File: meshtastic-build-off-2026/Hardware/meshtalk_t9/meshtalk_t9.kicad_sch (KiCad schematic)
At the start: 0 parts

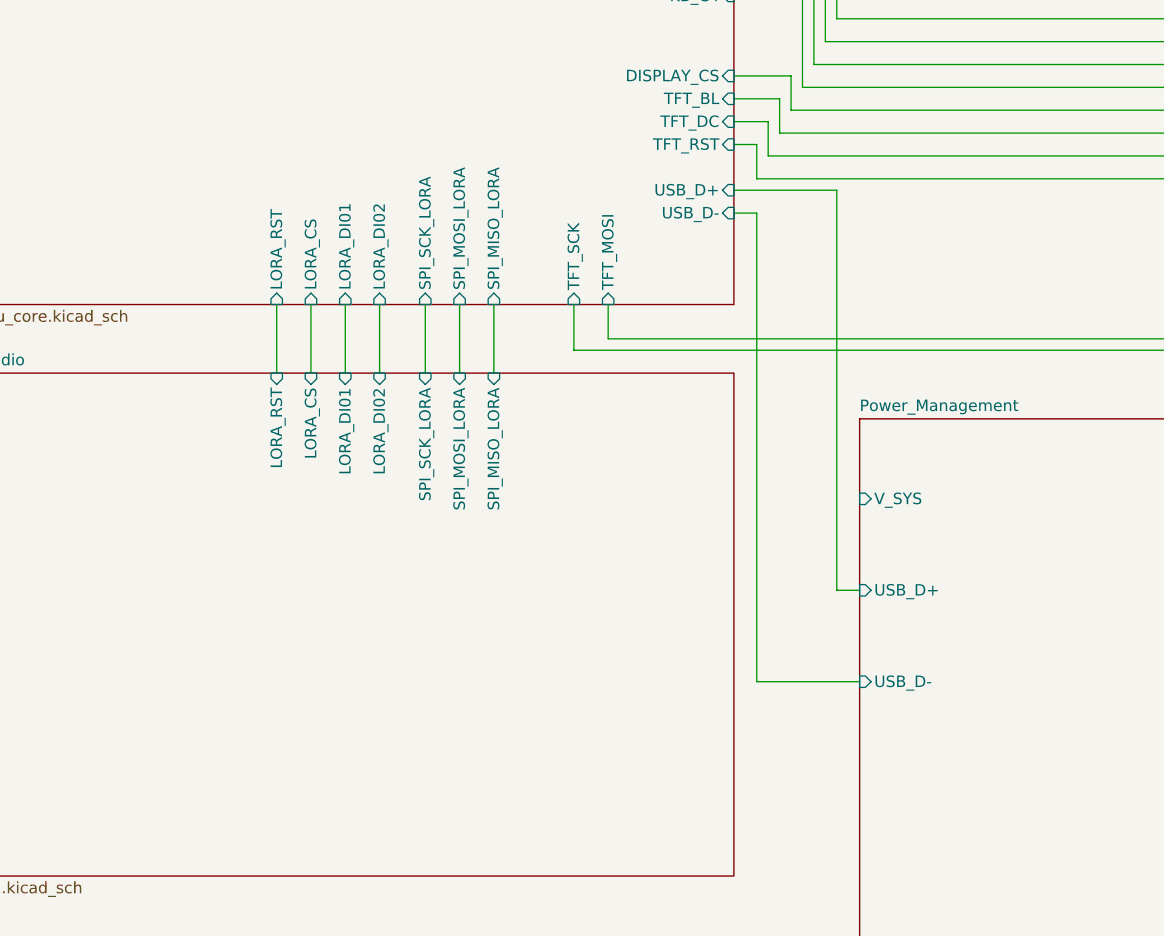
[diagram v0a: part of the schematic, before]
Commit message: rename + battery % + boot btn changed to reset + fix battery chrging
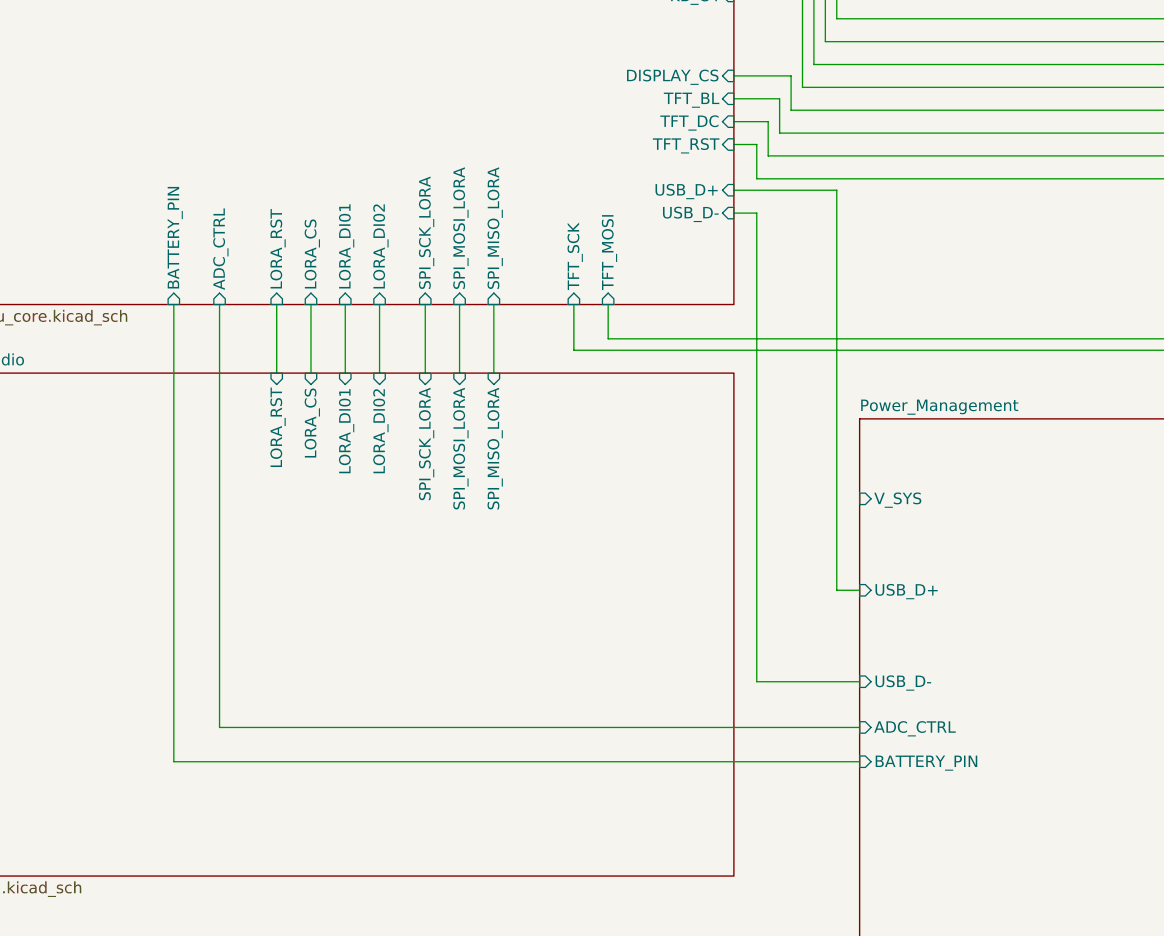
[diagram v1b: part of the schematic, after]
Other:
- sheet MCU_Core ports: added ADC_CTRL, BATTERY_PIN; removed none
- sheet Power_Management ports: added ADC_CTRL, BATTERY_PIN; removed none
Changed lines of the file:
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@@
+	(wire
+		(pts
+			(xy 39.37 121.92) (xy 115.57 121.92)
+		)
+		(stroke
+			(width 0)
+			(type default)
+		)
+	)
+	(wire
+		(pts
+			(xy 44.45 71.12) (xy 44.45 118.11)
+		)
+		(stroke
+			(width 0)
+			(type default)
+		)
+	)
 	(wire
 		(pts
@@
 	(wire
 		(pts
+			(xy 39.37 71.12) (xy 39.37 121.92)
+		)
+		(stroke
+			(width 0)
+			(type default)
+		)
+	)
+	(wire
+		(pts
 			(xy 110.49 34.29) (xy 101.6 34.29)
 		)
@@
 		(pts
 			(xy 114.3 36.83) (xy 172.72 36.83)
+		)
+		(stroke
+			(width 0)
+			(type default)
+		)
+	)
+	(wire
+		(pts
+			(xy 44.45 118.11) (xy 115.57 118.11)
 		)
 		(stroke
@@
 			)
 		)
+		(pin "BATTERY_PIN" input
+			(at 115.57 121.92 180)
+			(effects
+				(font
+					(size 1.27 1.27)
+				)
+				(justify left)
+			)
+		)
+		(pin "ADC_CTRL" input
+			(at 115.57 118.11 180)
+			(effects
+				(font
+					(size 1.27 1.27)
+				)
+				(justify left)
+			)
+		)
 		(instances
 			(project "Untitled"
@@
 			(effects
 				(font
+					(size 1.27 1.27)
+				)
+				(justify left)
+			)
+		)
+		(pin "ADC_CTRL" input
+			(at 44.45 71.12 270)
+			(effects
+				(font
+					(size 1.27 1.27)
+				)
+				(justify left)
+			)
+		)
+		(pin "BATTERY_PIN" input
+			(at 39.37 71.12 270)
+			(effects
+				(font

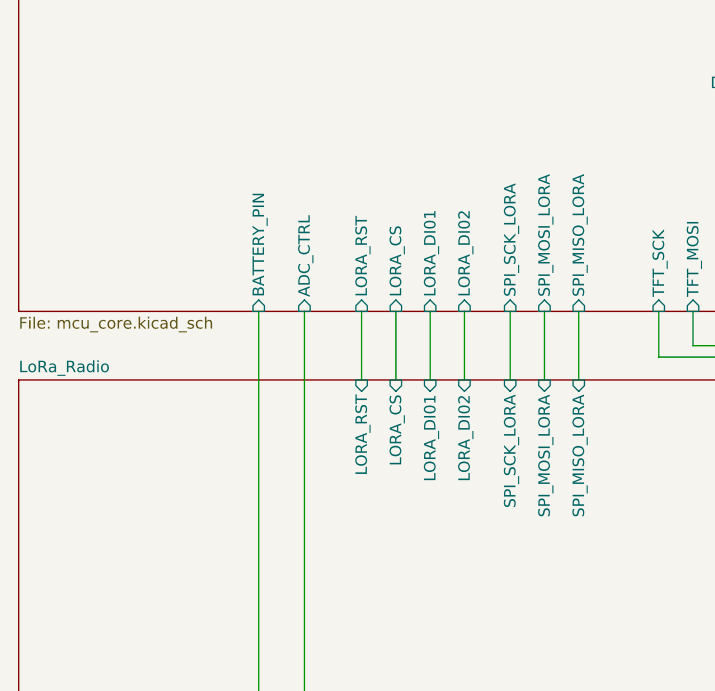
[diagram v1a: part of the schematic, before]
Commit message: Replace AP2112K-3.3  with AP7361C-33E Connected LORA RF_SW1 to GPIO Added ESD Added mounting holes for display (Waveshare 2 inch) Added Boot and Reset buttons made power rails thicker added dedicated layer for 3v3 and GND
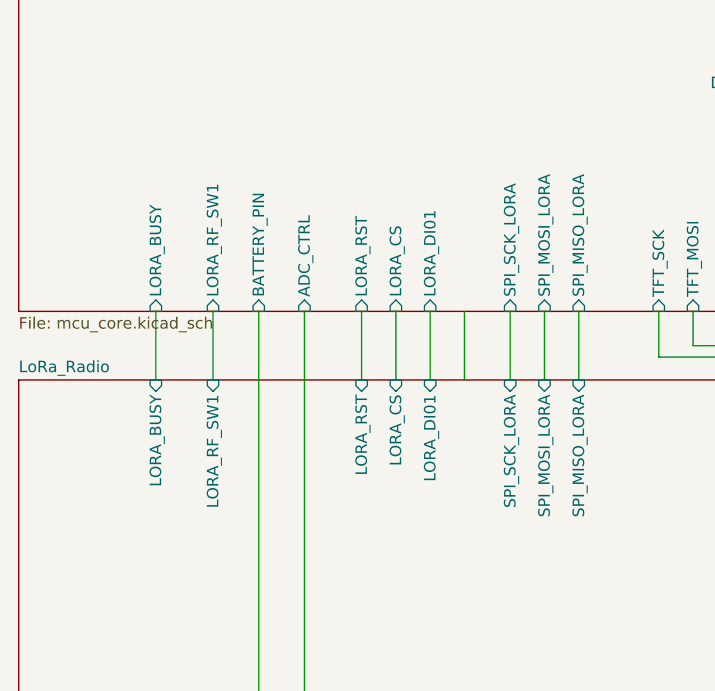
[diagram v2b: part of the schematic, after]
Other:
- sheet LoRa_Radio ports: added LORA_BUSY, LORA_RF_SW1; removed LORA_DI02
- sheet MCU_Core ports: added LORA_BUSY, LORA_RF_SW1; removed LORA_DI02
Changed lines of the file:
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@@
+	(wire
+		(pts
+			(xy 27.94 71.12) (xy 27.94 78.74)
+		)
+		(stroke
+			(width 0)
+			(type default)
+		)
+	)
 	(wire
 		(pts
@@
 		(pts
 			(xy 116.84 21.59) (xy 101.6 21.59)
+		)
+		(stroke
+			(width 0)
+			(type default)
+		)
+	)
+	(wire
+		(pts
+			(xy 34.29 71.12) (xy 34.29 78.74)
 		)
 		(stroke
@@
 			)
 		)
-		(pin "LORA_DI02" input
-			(at 62.23 78.74 90)
-			(effects
-				(font
-					(size 1.27 1.27)
-				)
-				(justify right)
-			)
-		)
 		(pin "LORA_DI01" input
 			(at 58.42 78.74 90)
@@
 			)
 		)
+		(pin "LORA_RF_SW1" input
+			(at 34.29 78.74 90)
+			(effects
+				(font
+					(size 1.27 1.27)
+				)
+				(justify right)
+			)
+		)
+		(pin "LORA_BUSY" input
+			(at 27.94 78.74 90)
+			(effects
+				(font
+					(size 1.27 1.27)
+				)
+				(justify right)
+			)
+		)
 		(instances
-			(project "Untitled"
+			(project "meshtalk_t9"
 				(path "/81d8a60b-fb85-4750-b4ba-90a418a69e1e"
 					(page "4")
@@
 		)
 		(instances
-			(project "Untitled"
+			(project "meshtalk_t9"
 				(path "/81d8a60b-fb85-4750-b4ba-90a418a69e1e"
 					(page "5")
@@
 		)
 		(instances
-			(project "Untitled"
+			(project "meshtalk_t9"
 				(path "/81d8a60b-fb85-4750-b4ba-90a418a69e1e"
 					(page "3")
@@
 			)
 		)
-		(pin "LORA_DI02" input
-			(at 62.23 71.12 270)
-			(effects
-				(font
-					(size 1.27 1.27)
-				)
-				(justify left)
-			)
-		)
 		(pin "KB_R1" input
 			(at 101.6 19.05 0)
@@
 			)
 		)
+		(pin "LORA_RF_SW1" input
+			(at 34.29 71.12 270)
+			(effects
+				(font
+					(size 1.27 1.27)
+				)
+				(justify left)
+			)
+		)
+		(pin "LORA_BUSY" input
+			(at 27.94 71.12 270)
+			(effects
+				(font
+					(size 1.27 1.27)
+				)
+				(justify left)
+			)
+		)
 		(instances
-			(project "Untitled"
+			(project "meshtalk_t9"
 				(path "/81d8a60b-fb85-4750-b4ba-90a418a69e1e"
 					(page "2")

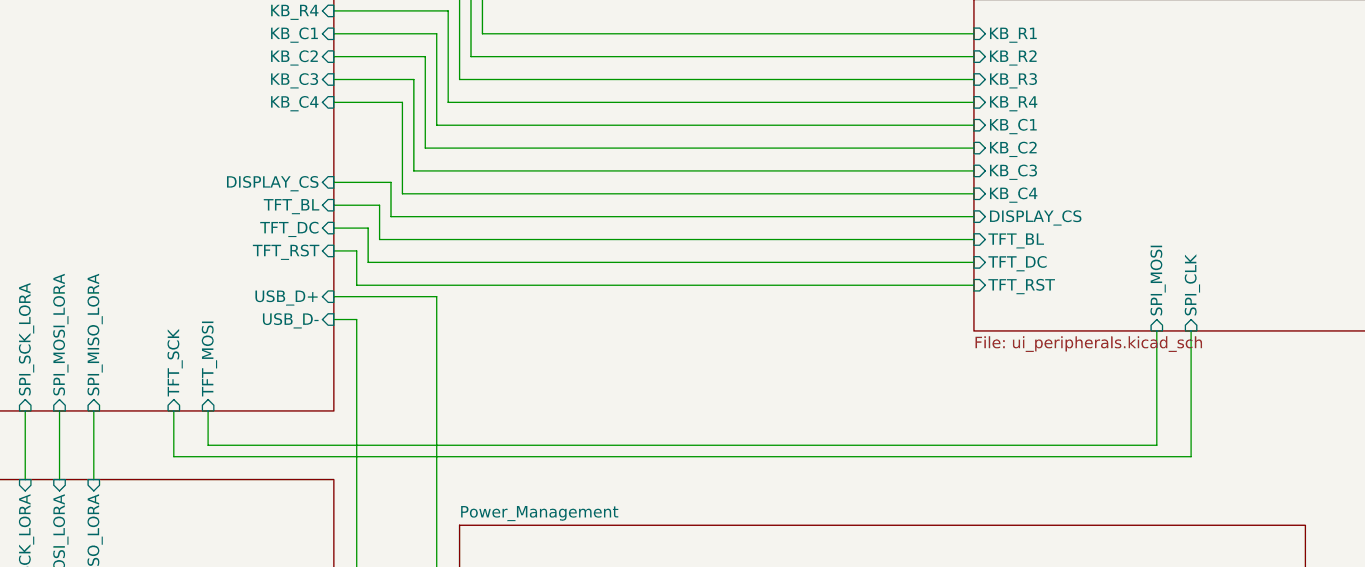
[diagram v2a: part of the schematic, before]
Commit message: PCB Updates - Align net names Clearence for esp32 antenna
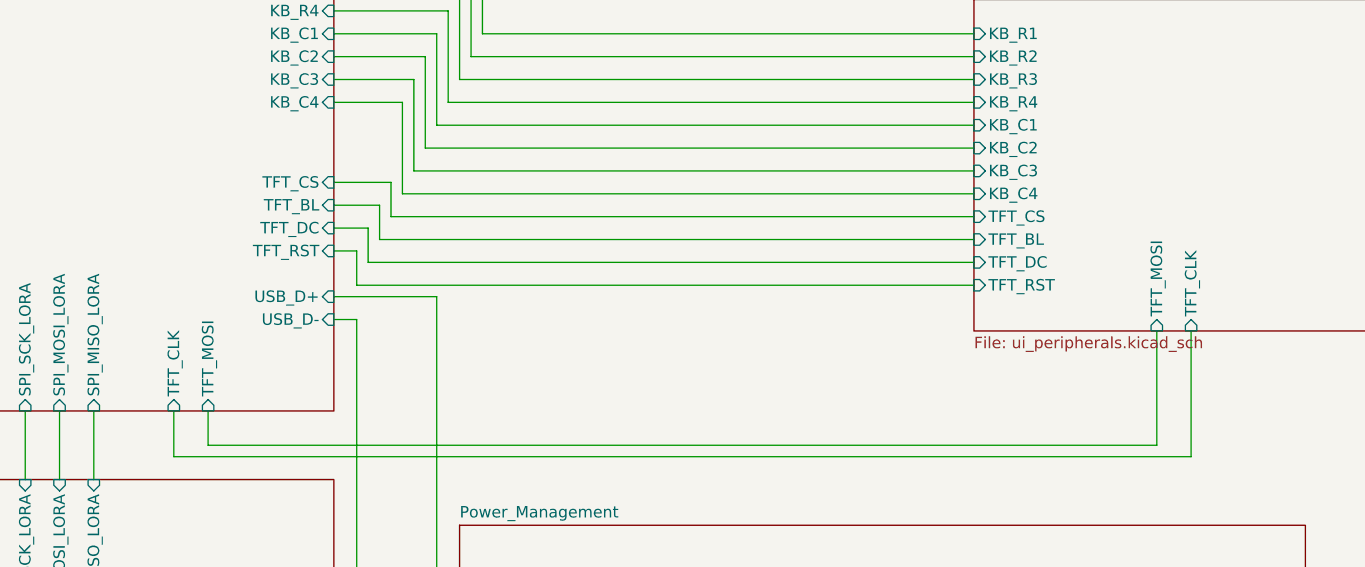
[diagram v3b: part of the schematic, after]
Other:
- sheet MCU_Core ports: added TFT_CLK, TFT_CS; removed DISPLAY_CS, TFT_SCK
- sheet User_Interface ports: added TFT_CLK, TFT_CS, TFT_MOSI; removed DISPLAY_CS, SPI_CLK, SPI_MOSI
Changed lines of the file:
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@@
-			)
-		)
-		(pin "SPI_MOSI" input
-			(at 193.04 62.23 270)
-			(effects
-				(font
-					(size 1.27 1.27)
-				)
-				(justify left)
 			)
 		)
@@
 			)
 		)
-		(pin "DISPLAY_CS" input
-			(at 172.72 49.53 180)
-			(effects
-				(font
-					(size 1.27 1.27)
-				)
-				(justify left)
-			)
-		)
 		(pin "TFT_BL" input
 			(at 172.72 52.07 180)
@@
 			)
 		)
-		(pin "SPI_CLK" input
+		(pin "TFT_MOSI" input
+			(at 193.04 62.23 270)
+			(effects
+				(font
+					(size 1.27 1.27)
+				)
+				(justify left)
+			)
+		)
+		(pin "TFT_CLK" input
 			(at 196.85 62.23 270)
+			(effects
+				(font
+					(size 1.27 1.27)
+				)
+				(justify left)
+			)
+		)
+		(pin "TFT_CS" input
+			(at 172.72 49.53 180)
 			(effects
 				(font
@@
 			)
 		)
-		(pin "DISPLAY_CS" input
-			(at 101.6 45.72 0)
-			(effects
-				(font
-					(size 1.27 1.27)
-				)
-				(justify right)
-			)
-		)
 		(pin "TFT_BL" input
 			(at 101.6 48.26 0)
@@
 			)
 		)
-		(pin "TFT_SCK" input
-			(at 83.82 71.12 270)
-			(effects
-				(font
-					(size 1.27 1.27)
-				)
-				(justify left)
-			)
-		)
 		(pin "SPI_SCK_LORA" input
 			(at 67.31 71.12 270)
@@
 			)
 		)
+		(pin "TFT_CLK" input
+			(at 83.82 71.12 270)
+			(effects
+				(font
+					(size 1.27 1.27)
+				)
+				(justify left)
+			)
+		)
+		(pin "TFT_CS" input
+			(at 101.6 45.72 0)
+			(effects
+				(font
+					(size 1.27 1.27)
+				)
+				(justify right)
+			)
+		)
